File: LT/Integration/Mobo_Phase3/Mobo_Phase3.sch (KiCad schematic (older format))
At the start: 1 part, among them J1 Bus

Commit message: Fixed phase 3 integration folder for Mobo
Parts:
- J1: symbol Mobo_Dev1-rescue:Bus-SS -> Mobo_Phase3-rescue:Bus-SS
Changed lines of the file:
@@
 EESchema Schematic File Version 4
-LIBS:Mobo_Dev1-cache
+LIBS:Mobo_Phase3-cache
 EELAYER 26 0
 EELAYER END
@@
 Transmitting Stage
 $Comp
-L Mobo_Dev1-rescue:Bus-SS J1
+L Mobo_Phase3-rescue:Bus-SS J1
 U 1 1 5EA20A51
 P 13050 3300
@@
 $EndComp
 $Comp
-L Mobo_Dev1-rescue:Bus-SS J1
+L Mobo_Phase3-rescue:Bus-SS J1
 U 2 1 5EA309D4
 P 13050 4100
@@
 $EndComp
 $Comp
-L Mobo_Dev1-rescue:Bus-SS J1
+L Mobo_Phase3-rescue:Bus-SS J1
 U 3 1 5EA3AF6E
 P 13050 4900
@@
 $EndComp
 $Comp
-L Mobo_Dev1-rescue:Bus-SS J1
+L Mobo_Phase3-rescue:Bus-SS J1
 U 4 1 5EA3F11D
 P 13050 6200

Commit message: Annotated Phase 3 Motherboard Block Diagram
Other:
- note added: "29.4MHz_BPF\n"
- note added: "29.4MHz_LPF"
- note added: "Image Reject Filter"
- note added: "Low Noise Amplifier"
- note added: "Power Amplifier"
- note added: "Pre-Amplifier"
- note added: "Step-Daughter Board"
- note added: "Variable Attenuator"
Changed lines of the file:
@@
 F0 "Variable Attenuator" 50
 F1 "VA.sch" 50
+F2 "VA_OUT" O R 3450 2250 50
 $EndSheet
 $Sheet
@@
 F0 "Image Reject Filter" 50
 F1 "ImageReject.sch" 50
+F2 "IR_IN" I L 4450 2250 50
+F3 "IR_OUT" O R 5750 2250 50
 $EndSheet
 $Sheet
@@
 F0 "Low Noise Amplifier" 50
 F1 "LNA.sch" 50
+F2 "LNA_IN" I L 6850 2250 50
 $EndSheet
 $Sheet
@@
 F0 "29.4 MHz Bandpass Filter" 50
 F1 "29_4_BPF.sch" 50
+F2 "29.4BPF_OUT" O R 2850 4950 50
 $EndSheet
 $Sheet
@@
 F0 "Pre Amplifier" 50
 F1 "PreAmp.sch" 50
+F2 "PRE-AMP_IN" I L 3650 4950 50
+F3 "PRE-AMP_OUT" O R 5050 4950 50
 $EndSheet
 $Sheet
@@
 F0 "Power Amplifier" 50
 F1 "PowerAmplifier.sch" 50
+F2 "PA_IN" I L 5800 4950 50
+F3 "PA_OUT" O R 7250 4950 50
 $EndSheet
 $Sheet
@@
 F0 "Low Pass Filter" 50
 F1 "LowPassFiter.sch" 50
+F2 "29.4LPF_IN" I L 7750 4950 50
 $EndSheet
 Wire Notes Line width 39 style solid
@@
 Text Notes 12900 1600 0    197  ~ 39
 Bus
+Wire Wire Line
+	2850 4950 3650 4950
+Wire Wire Line
+	7250 4950 7750 4950
+Wire Wire Line
+	5800 4950 5050 4950
+Wire Notes Line width 10 rgb(72, 0, 0)
+	5700 4300 7350 4300
+Wire Notes Line width 10 rgb(72, 0, 0)
+	7350 4300 7350 5550
+Wire Notes Line width 10 rgb(72, 0, 0)
+	7350 5550 5700 5550
+Wire Notes Line width 10 rgb(72, 0, 0)
+	5700 5550 5700 4300
+Text Notes 5700 5750 0    100  ~ 20
+Step-Daughter Board
+Wire Wire Line
+	4450 2250 3450 2250
+Wire Wire Line
+	5750 2250 6850 2250
+Text Notes 1700 4300 0    100  ~ 20
+29.4MHz_BPF\n
+Text Notes 3900 4300 0    100  ~ 20
+Pre-Amplifier
+Text Notes 5950 4250 0    100  ~ 20
+Power Amplifier
+Text Notes 7950 4350 0    100  ~ 20
+29.4MHz_LPF
+Text Notes 2150 1750 0    100  ~ 20
+Variable Attenuator
+Text Notes 4400 1700 0    100  ~ 20
+Image Reject Filter
+Text Notes 6800 1700 0    100  ~ 20
+Low Noise Amplifier
 $EndSCHEMATC

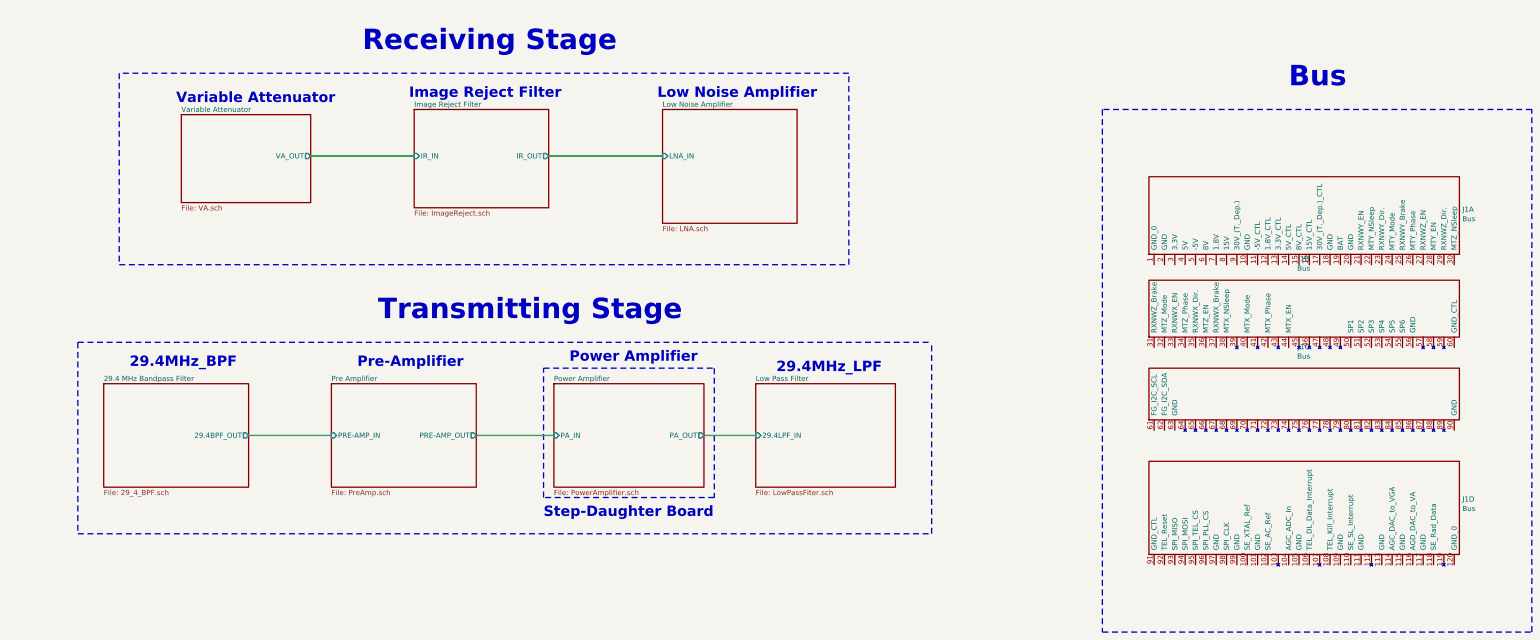
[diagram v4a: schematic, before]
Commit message: Fixed the hierarchy for the MoBo Phase 3
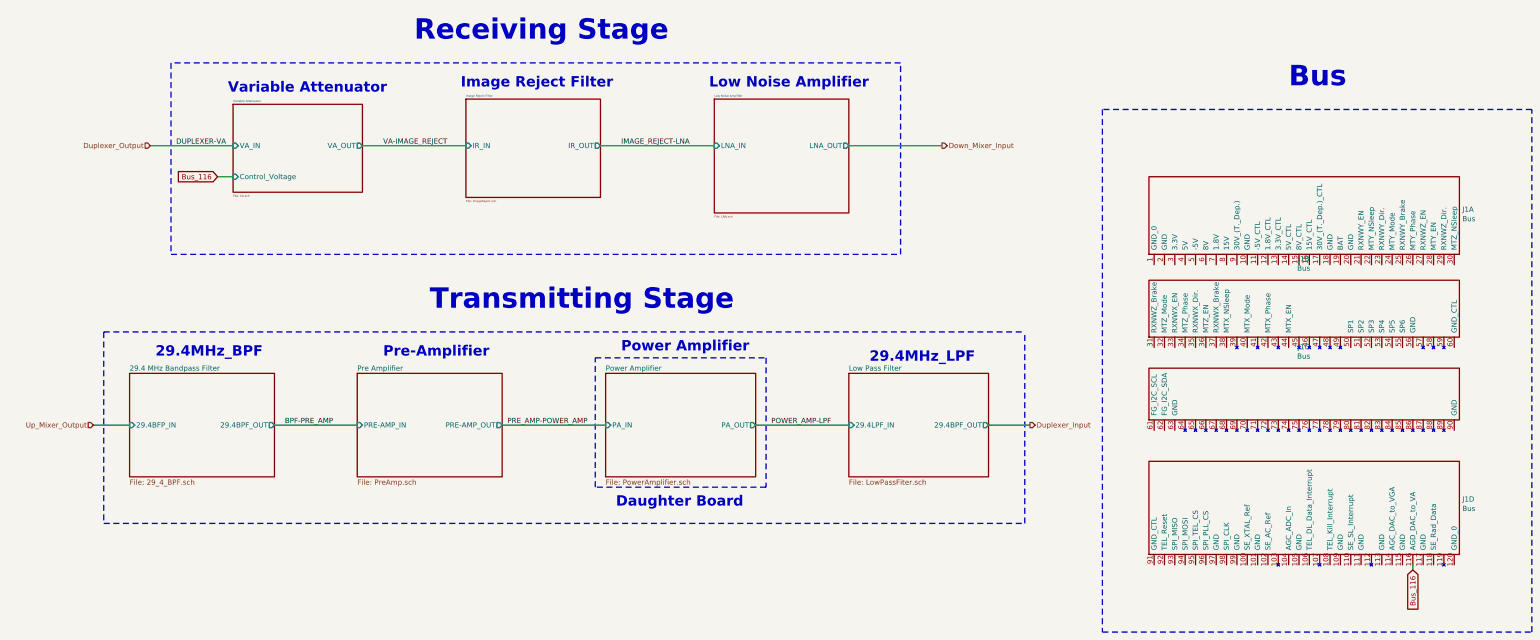
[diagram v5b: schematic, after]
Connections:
- net Bus_116: now reaches J1.116 (AGD_DAC_to_VA)
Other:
- note added: "Daughter Board"
- note removed: "Step-Daughter Board"
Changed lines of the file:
@@
 EESchema Schematic File Version 4
-LIBS:Mobo_Phase3-cache
-EELAYER 26 0
+EELAYER 30 0
 EELAYER END
 $Descr A3 16535 11693
@@
 $EndDescr
 $Sheet
-S 2200 1850 1250 850
+S 2700 1750 1250 850
 U 5E9B72A2
-F0 "Variable Attenuator" 50
-F1 "VA.sch" 50
-F2 "VA_OUT" O R 3450 2250 50
-$EndSheet
-$Sheet
-S 4450 1800 1300 950
+F0 "Variable Attenuator" 20
+F1 "VA.sch" 20
+F2 "VA_OUT" O R 3950 2150 50
+F3 "VA_IN" I L 2700 2150 50
+F4 "Control_Voltage" I L 2700 2450 50
+$EndSheet
+$Sheet
+S 4950 1700 1300 950
 U 5E9B72E0
-F0 "Image Reject Filter" 50
-F1 "ImageReject.sch" 50
-F2 "IR_IN" I L 4450 2250 50
-F3 "IR_OUT" O R 5750 2250 50
-$EndSheet
-$Sheet
-S 6850 1800 1300 1100
-U 5E9B734B
-F0 "Low Noise Amplifier" 50
-F1 "LNA.sch" 50
-F2 "LNA_IN" I L 6850 2250 50
-$EndSheet
-$Sheet
-S 1450 4450 1400 1000
+F0 "Image Reject Filter" 20
+F1 "ImageReject.sch" 20
+F2 "IR_IN" I L 4950 2150 50
+F3 "IR_OUT" O R 6250 2150 50
+$EndSheet
+$Sheet
+S 1700 4350 1400 1000
 U 5E9B7D55
 F0 "29.4 MHz Bandpass Filter" 50
 F1 "29_4_BPF.sch" 50
-F2 "29.4BPF_OUT" O R 2850 4950 50
-$EndSheet
-$Sheet
-S 3650 4450 1400 1000
+F2 "29.4BPF_OUT" O R 3100 4850 50
+F3 "29.4BFP_IN" I L 1700 4850 50
+$EndSheet
+$Sheet
+S 3900 4350 1400 1000
 U 5E9B7D7E
 F0 "Pre Amplifier" 50
 F1 "PreAmp.sch" 50
-F2 "PRE-AMP_IN" I L 3650 4950 50
-F3 "PRE-AMP_OUT" O R 5050 4950 50
-$EndSheet
-$Sheet
-S 5800 4450 1450 1000
+F2 "PRE-AMP_IN" I L 3900 4850 50
+F3 "PRE-AMP_OUT" O R 5300 4850 50
+$EndSheet
+$Sheet
+S 6300 4350 1450 1000
 U 5E9B7DCF
 F0 "Power Amplifier" 50
 F1 "PowerAmplifier.sch" 50
-F2 "PA_IN" I L 5800 4950 50
-F3 "PA_OUT" O R 7250 4950 50
-$EndSheet
-$Sheet
-S 7750 4450 1350 1000
+F2 "PA_IN" I L 6300 4850 50
+F3 "PA_OUT" O R 7750 4850 50
+$EndSheet
+$Sheet
+S 8650 4350 1350 1000
 U 5E9B7E58
 F0 "Low Pass Filter" 50
 F1 "LowPassFiter.sch" 50
-F2 "29.4LPF_IN" I L 7750 4950 50
-$EndSheet
-Wire Notes Line width 39 style solid
-	1600 1450 1600 3300
-Wire Notes Line width 39 style solid
-	1600 3300 8650 3300
-Wire Notes Line width 39 style solid
-	8650 3300 8650 1450
-Wire Notes Line width 39 style solid
-	8650 1450 1600 1450
-Wire Notes Line width 39 style solid rgb(0, 194, 0)
-	1200 4050 1200 5900
-Wire Notes Line width 39 style solid rgb(0, 194, 0)
-	9450 5900 9450 4050
-Wire Notes Line width 39 style solid rgb(0, 194, 0)
-	1200 5900 9450 5900
-Wire Notes Line width 39 style solid rgb(0, 194, 0)
-	1200 4050 9450 4050
-Text Notes 3950 1250 0    197  ~ 39
+F2 "29.4LPF_IN" I L 8650 4850 50
+F3 "29.4BPF_OUT" O R 10000 4850 50
+$EndSheet
+Wire Notes Line width 39 style solid
+	2100 1350 2100 3200
+Wire Notes Line width 39 style solid
+	2100 3200 9150 3200
+Wire Notes Line width 39 style solid
+	9150 3200 9150 1350
+Wire Notes Line width 39 style solid
+	9150 1350 2100 1350
+Wire Notes Line width 39 style solid rgb(0, 194, 0)
+	1450 3950 1450 5800
+Wire Notes Line width 39 style solid rgb(0, 194, 0)
+	10350 5800 10350 3950
+Text Notes 4450 1150 0    197  ~ 39
 Receiving Stage
-Text Notes 4100 3850 0    197  ~ 39
+Text Notes 4600 3750 0    197  ~ 39
 Transmitting Stage
 $Comp
@@
 Bus
 Wire Wire Line
-	2850 4950 3650 4950
-Wire Wire Line
-	7250 4950 7750 4950
-Wire Wire Line
-	5800 4950 5050 4950
-Wire Notes Line width 10 rgb(72, 0, 0)
-	5700 4300 7350 4300
-Wire Notes Line width 10 rgb(72, 0, 0)
-	7350 4300 7350 5550
-Wire Notes Line width 10 rgb(72, 0, 0)
-	7350 5550 5700 5550
-Wire Notes Line width 10 rgb(72, 0, 0)
-	5700 5550 5700 4300
-Text Notes 5700 5750 0    100  ~ 20
-Step-Daughter Board
-Wire Wire Line
-	4450 2250 3450 2250
-Wire Wire Line
-	5750 2250 6850 2250
-Text Notes 1700 4300 0    100  ~ 20
+	3100 4850 3900 4850
+Wire Notes Line width 10 rgb(72, 0, 0)
+	6200 4200 7850 4200
+Wire Notes Line width 10 rgb(72, 0, 0)
+	7850 4200 7850 5450
+Wire Notes Line width 10 rgb(72, 0, 0)
+	7850 5450 6200 5450
+Wire Notes Line width 10 rgb(72, 0, 0)
+	6200 5450 6200 4200
+Text Notes 6400 5650 0    100  ~ 20
+Daughter Board
+Wire Wire Line
+	4950 2150 3950 2150
+Wire Wire Line
+	6250 2150 7350 2150
+Text Notes 1950 4200 0    100  ~ 20
 29.4MHz_BPF\n
-Text Notes 3900 4300 0    100  ~ 20
+Text Notes 4150 4200 0    100  ~ 20
 Pre-Amplifier
-Text Notes 5950 4250 0    100  ~ 20
+Text Notes 6450 4150 0    100  ~ 20
 Power Amplifier
-Text Notes 7950 4350 0    100  ~ 20
+Text Notes 8850 4250 0    100  ~ 20
 29.4MHz_LPF
-Text Notes 2150 1750 0    100  ~ 20
+Text Notes 2650 1650 0    100  ~ 20
 Variable Attenuator
-Text Notes 4400 1700 0    100  ~ 20
+Text Notes 4900 1600 0    100  ~ 20
 Image Reject Filter
-Text Notes 6800 1700 0    100  ~ 20
+Text Notes 7300 1600 0    100  ~ 20
 Low Noise Amplifier
+Text Label 4150 2150 0    50   ~ 0
+VA-IMAGE_REJECT
+Text Label 6450 2150 0    50   ~ 0
+IMAGE_REJECT-LNA
+Text HLabel 9550 2150 2    50   Output ~ 0
+Down_Mixer_Input
+$Sheet
+S 7350 1700 1300 1100
+U 5E9B734B
+F0 "Low Noise Amplifier" 20
+F1 "LNA.sch" 20
+F2 "LNA_IN" I L 7350 2150 50
+F3 "LNA_OUT" O R 8650 2150 50
+$EndSheet
+Wire Wire Line
+	8650 2150 9550 2150
+Text HLabel 1900 2150 0    50   Input ~ 0
+Duplexer_Output
+Wire Wire Line
+	1900 2150 2700 2150
+Text Label 2150 2150 0    50   ~ 0
+DUPLEXER-VA
+Text Label 3200 4850 0    50   ~ 0
+BPF-PRE_AMP
+Text Label 5350 4850 0    50   ~ 0
+PRE_AMP-POWER_AMP
+Wire Wire Line
+	5300 4850 6300 4850
+Text HLabel 1350 4850 0    50   Input ~ 0
+Up_Mixer_Output
+Wire Wire Line
+	1350 4850 1700 4850
+Text Label 7900 4850 0    50   ~ 0
+POWER_AMP-LPF
+Wire Wire Line
+	7750 4850 8650 4850
+Wire Notes Line width 39 style solid rgb(0, 194, 0)
+	1450 3950 10350 3950
+Wire Notes Line width 39 style solid rgb(0, 194, 0)
+	1450 5800 10350 5800
+Text HLabel 10400 4850 2    50   Output ~ 0
+Duplexer_Input
+Wire Wire Line
+	10000 4850 10400 4850
+Text GLabel 2550 2450 0    50   Input ~ 0
+Bus_116
+Wire Wire Line
+	2550 2450 2700 2450
+Text GLabel 14100 6250 3    50   Input ~ 0
+Bus_116
+Wire Wire Line
+	14100 6250 14100 6200
 $EndSCHEMATC

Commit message: Added the finalized layouts for the Mobo and Dobo Phase 3, as well as the preliminary layout for Phase 4 of both boards
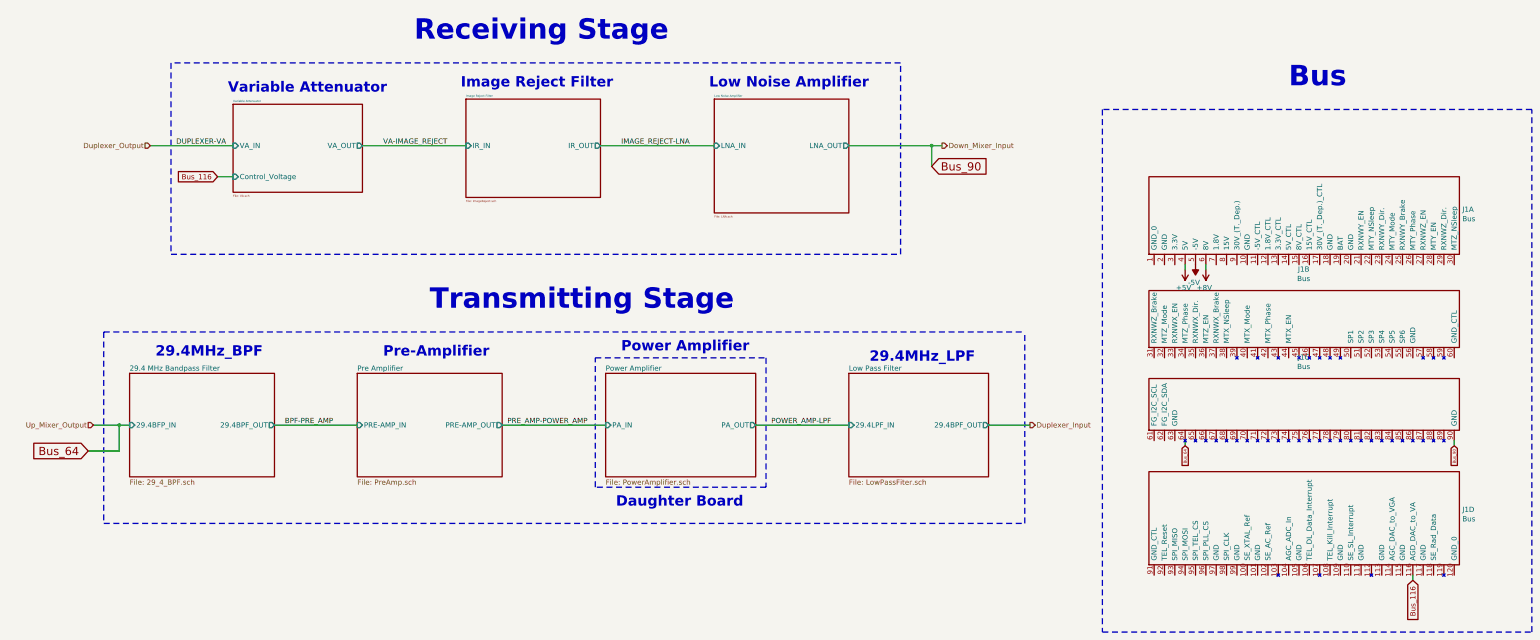
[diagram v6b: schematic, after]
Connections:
- net +5V: now reaches J1.4 (5V)
- net -5V: now reaches J1.5 (-5V)
- net +8V: now reaches J1.6 (8V)
- net Bus_64: now reaches J1.64
- net Bus_90: now reaches J1.90 (GND)
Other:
- moved on the sheet: J1B, J1C, J1D
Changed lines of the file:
@@
-	1    0    0    -1
-$EndComp
-$Comp
-L Mobo_Phase3-rescue:Bus-SS J1
-U 2 1 5EA309D4
-P 13050 4100
-F 0 "J1" H 13045 4956 50  0000 C CNN
-F 1 "Bus" H 13045 4865 50  0000 C CNN
-F 2 "SS:STD_PCB_A1_v1.1" H 11750 5150 50  0001 C CNN
-F 3 "" H 11750 5150 50  0001 C CNN
-	2    13050 4100
-	1    0    0    -1
-$EndComp
-$Comp
-L Mobo_Phase3-rescue:Bus-SS J1
-U 3 1 5EA3AF6E
-P 13050 4900
-F 0 "J1" H 13045 5706 50  0000 C CNN
-F 1 "Bus" H 13045 5615 50  0000 C CNN
-F 2 "SS:STD_PCB_A1_v1.1" H 11750 5950 50  0001 C CNN
-F 3 "" H 11750 5950 50  0001 C CNN
-	3    13050 4900
-	1    0    0    -1
-$EndComp
-$Comp
-L Mobo_Phase3-rescue:Bus-SS J1
-U 4 1 5EA3F11D
-P 13050 6200
-F 0 "J1" H 14578 6834 50  0000 L CNN
-F 1 "Bus" H 14578 6743 50  0000 L CNN
-F 2 "SS:STD_PCB_A1_v1.1" H 11750 7250 50  0001 C CNN
-F 3 "" H 11750 7250 50  0001 C CNN
-	4    13050 6200
 	1    0    0    -1
 $EndComp
@@
 $EndSheet
 Wire Wire Line
-	8650 2150 9550 2150
+	8650 2150 9450 2150
 Text HLabel 1900 2150 0    50   Input ~ 0
 Duplexer_Output
@@
 Up_Mixer_Output
 Wire Wire Line
-	1350 4850 1700 4850
+	1350 4850 1600 4850
 Text Label 7900 4850 0    50   ~ 0
 POWER_AMP-LPF
@@
 Wire Wire Line
 	2550 2450 2700 2450
-Text GLabel 14100 6250 3    50   Input ~ 0
+Text GLabel 14100 6350 3    50   Input ~ 0
 Bus_116
 Wire Wire Line
-	14100 6250 14100 6200
+	14100 6350 14100 6300
+$Comp
+L power:+8V #PWR0127
+U 1 1 5ED1ACEA
+P 12100 3350
+F 0 "#PWR0127" H 12100 3200 50  0001 C CNN
+F 1 "+8V" H 12115 3523 50  0000 C CNN
+F 2 "" H 12100 3350 50  0001 C CNN
+F 3 "" H 12100 3350 50  0001 C CNN
+	1    12100 3350
+	-1   0    0    1
+$EndComp
+$Comp
+L power:+5V #PWR0128
+U 1 1 5ED1BF87
+P 11900 3350
+F 0 "#PWR0128" H 11900 3200 50  0001 C CNN
+F 1 "+5V" H 11915 3523 50  0000 C CNN
+F 2 "" H 11900 3350 50  0001 C CNN
+F 3 "" H 11900 3350 50  0001 C CNN
+	1    11900 3350
+	-1   0    0    1
+$EndComp
+$Comp
+L power:-5V #PWR0129
+U 1 1 5ED1C9AA
+P 12000 3300
+F 0 "#PWR0129" H 12000 3400 50  0001 C CNN
+F 1 "-5V" H 12015 3473 50  0000 C CNN
+F 2 "" H 12000 3300 50  0001 C CNN
+F 3 "" H 12000 3300 50  0001 C CNN
+	1    12000 3300
+	-1   0    0    1
+$EndComp
+Text GLabel 9450 2350 2    79   Input ~ 0
+Bus_90
+Wire Wire Line
+	9450 2350 9450 2150
+Connection ~ 9450 2150
+Wire Wire Line
+	9450 2150 9550 2150
+Text GLabel 1300 5100 0    79   Input ~ 0
+Bus_64
+Wire Wire Line
+	1300 5100 1600 5100
+Wire Wire Line
+	1600 5100 1600 4850
+Connection ~ 1600 4850
+Wire Wire Line
+	1600 4850 1700 4850
+Wire Wire Line
+	11900 5000 11900 5050
+Text GLabel 11900 5050 3    28   Input ~ 0
+Bus_64
+Wire Wire Line
+	14500 5000 14500 5050
+Text GLabel 14500 5050 3    28   Input ~ 0
+Bus_90
+$Comp
+L Mobo_Phase3-rescue:Bus-SS J1
+U 4 1 5EA3F11D
+P 13050 6300
+F 0 "J1" H 14578 6934 50  0000 L CNN
+F 1 "Bus" H 14578 6843 50  0000 L CNN
+F 2 "SS:STD_PCB_A1_v1.1" H 11750 7350 50  0001 C CNN
+F 3 "" H 11750 7350 50  0001 C CNN
+	4    13050 6300
+	1    0    0    -1
+$EndComp
+$Comp
+L Mobo_Phase3-rescue:Bus-SS J1
+U 3 1 5EA3AF6E
+P 13050 5000
+F 0 "J1" H 13045 5806 50  0000 C CNN
+F 1 "Bus" H 13045 5715 50  0000 C CNN
+F 2 "SS:STD_PCB_A1_v1.1" H 11750 6050 50  0001 C CNN
+F 3 "" H 11750 6050 50  0001 C CNN
+	3    13050 5000
+	1    0    0    -1
+$EndComp
+$Comp
+L Mobo_Phase3-rescue:Bus-SS J1
+U 2 1 5EA309D4
+P 13050 4200
+F 0 "J1" H 13045 5056 50  0000 C CNN
+F 1 "Bus" H 13045 4965 50  0000 C CNN
+F 2 "SS:STD_PCB_A1_v1.1" H 11750 5250 50  0001 C CNN
+F 3 "" H 11750 5250 50  0001 C CNN
+	2    13050 4200
+	1    0    0    -1
+$EndComp
+Wire Wire Line
+	11900 3300 11900 3350
+Wire Wire Line
+	12100 3300 12100 3350
 $EndSCHEMATC
